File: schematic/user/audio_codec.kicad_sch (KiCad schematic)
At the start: 27 parts, among them U4 TLV320AIC3254IRHBR

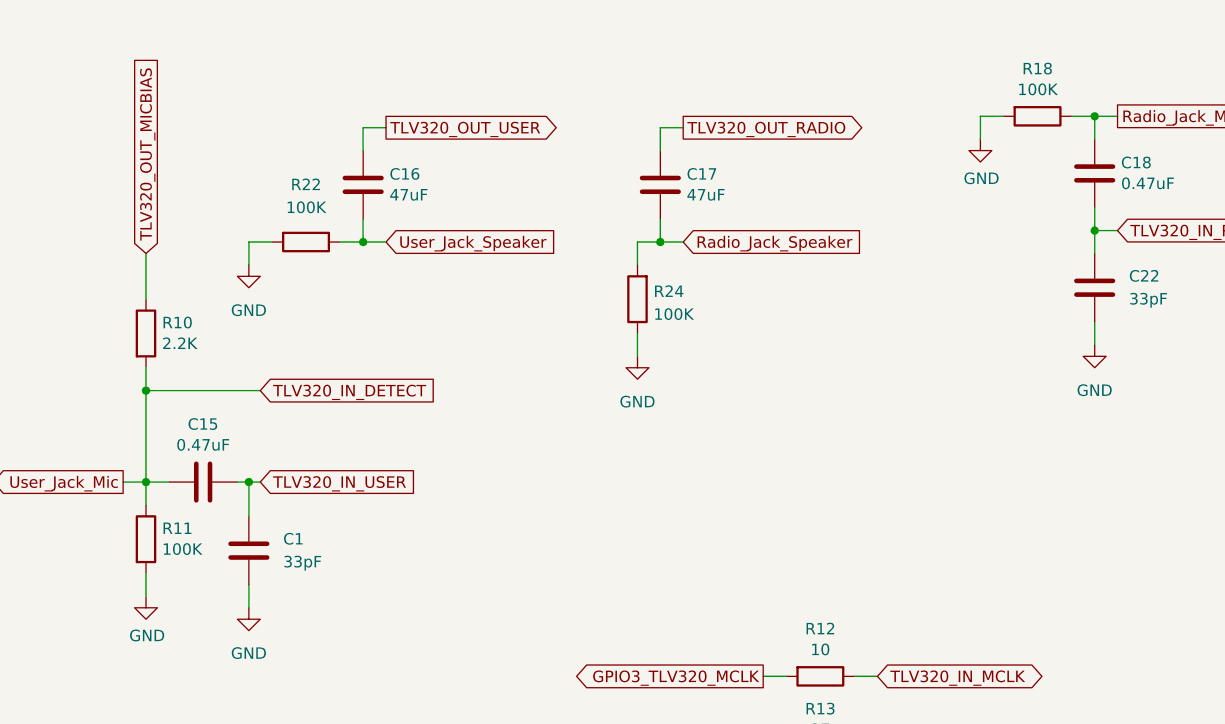
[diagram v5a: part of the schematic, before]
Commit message: v0.6 board: use 10K for audio pulldown resistors.
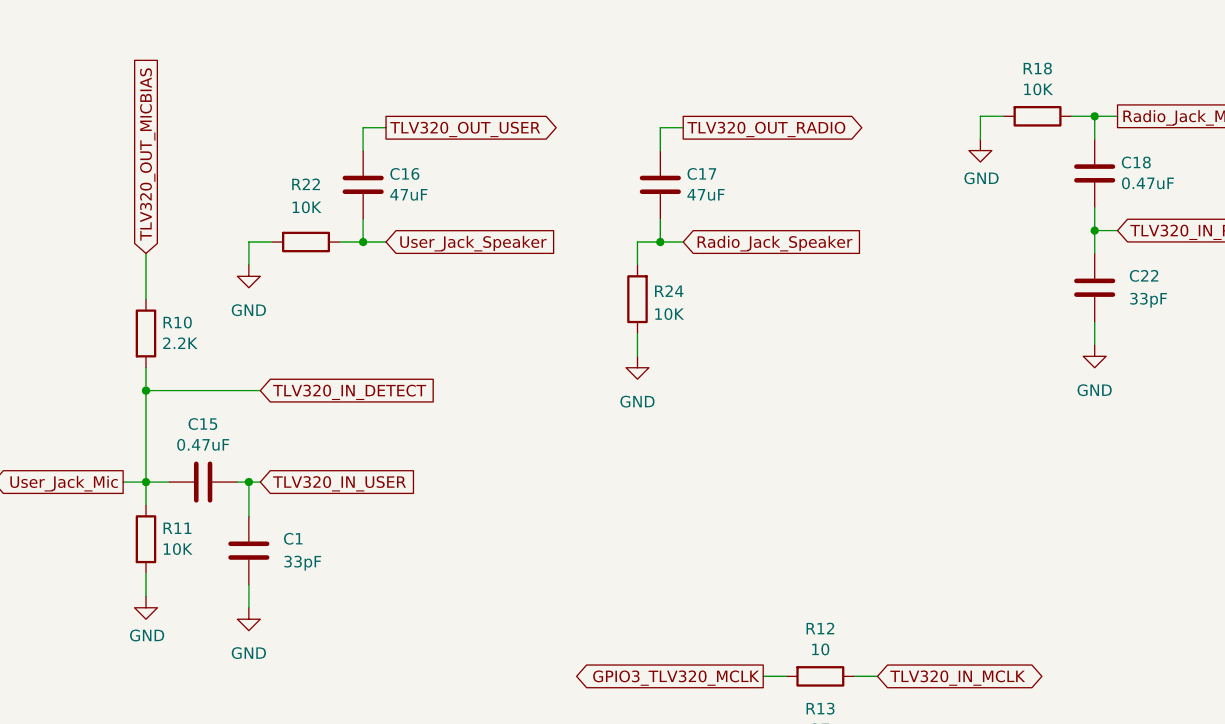
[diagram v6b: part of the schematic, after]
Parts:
- R11, R18, R22, R24: value 100K -> 10K; LCSC C25741 -> C25744
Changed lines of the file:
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@@
     (in_bom yes) (on_board yes) (fields_autoplaced)
     (property "Reference" "R22" (id 0) (at 167.64 35.56 90))
-    (property "Value" "100K" (id 1) (at 167.64 38.1 90))
+    (property "Value" "10K" (id 1) (at 167.64 38.1 90))
     (property "Footprint" "Resistor_SMD:R_0402_1005Metric" (id 2) (at 167.64 40.132 90)
       (effects (font (size 1.27 1.27)) hide)
     )
-    (property "Datasheet" "https://datasheet.lcsc.com/lcsc/2206010100_UNI-ROYAL-Uniroyal-Elec-0402WGF1003TCE_C25741.pdf" (id 3) (at 167.64 41.91 0)
-      (effects (font (size 1.27 1.27)) hide)
-    )
-    (property "LCSC" "C25741" (id 4) (at 167.64 41.91 0)
+    (property "Datasheet" "https://datasheet.lcsc.com/lcsc/2206010100_UNI-ROYAL-Uniroyal-Elec-0402WGF1002TCE_C25744.pdf" (id 3) (at 167.64 41.91 0)
+      (effects (font (size 1.27 1.27)) hide)
+    )
+    (property "LCSC" "C25744" (id 4) (at 167.64 41.91 0)
       (effects (font (size 1.27 1.27)) hide)
     )
@@
       (effects (font (size 1.27 1.27)) (justify right))
     )
-    (property "Value" "100K" (id 1) (at 206.248 49.9622 0)
+    (property "Value" "10K" (id 1) (at 206.248 49.9622 0)
       (effects (font (size 1.27 1.27)) (justify right))
     )
@@
       (effects (font (size 1.27 1.27)) hide)
     )
-    (property "Datasheet" "https://datasheet.lcsc.com/lcsc/2206010100_UNI-ROYAL-Uniroyal-Elec-0402WGF1003TCE_C25741.pdf" (id 3) (at 204.47 48.26 0)
-      (effects (font (size 1.27 1.27)) hide)
-    )
-    (property "LCSC" "C25741" (id 4) (at 204.47 48.26 0)
+    (property "Datasheet" "https://datasheet.lcsc.com/lcsc/2206010100_UNI-ROYAL-Uniroyal-Elec-0402WGF1002TCE_C25744.pdf" (id 3) (at 204.47 48.26 0)
+      (effects (font (size 1.27 1.27)) hide)
+    )
+    (property "LCSC" "C25744" (id 4) (at 204.47 48.26 0)
       (effects (font (size 1.27 1.27)) hide)
     )
@@
     (in_bom yes) (on_board yes)
     (property "Reference" "R18" (id 0) (at 248.92 22.6822 90))
-    (property "Value" "100K" (id 1) (at 248.92 24.9936 90))
+    (property "Value" "10K" (id 1) (at 248.92 24.9936 90))
     (property "Footprint" "Resistor_SMD:R_0402_1005Metric" (id 2) (at 248.92 26.162 90)
       (effects (font (size 1.27 1.27)) hide)
     )
-    (property "Datasheet" "https://datasheet.lcsc.com/lcsc/2206010100_UNI-ROYAL-Uniroyal-Elec-0402WGF1003TCE_C25741.pdf" (id 3) (at 248.92 27.94 0)
-      (effects (font (size 1.27 1.27)) hide)
-    )
-    (property "LCSC" "C25741" (id 4) (at 248.92 27.94 0)
+    (property "Datasheet" "https://datasheet.lcsc.com/lcsc/2206010100_UNI-ROYAL-Uniroyal-Elec-0402WGF1002TCE_C25744.pdf" (id 3) (at 248.92 27.94 0)
+      (effects (font (size 1.27 1.27)) hide)
+    )
+    (property "LCSC" "C25744" (id 4) (at 248.92 27.94 0)
       (effects (font (size 1.27 1.27)) hide)
     )
@@
       (effects (font (size 1.27 1.27)) (justify left))
     )
-    (property "Value" "100K" (id 1) (at 151.638 76.073 0)
+    (property "Value" "10K" (id 1) (at 151.638 76.073 0)
       (effects (font (size 1.27 1.27)) (justify left))
     )
@@
       (effects (font (size 1.27 1.27)) hide)
     )
-    (property "Datasheet" "https://datasheet.lcsc.com/lcsc/2206010100_UNI-ROYAL-Uniroyal-Elec-0402WGF1003TCE_C25741.pdf" (id 3) (at 149.86 74.93 0)
-      (effects (font (size 1.27 1.27)) hide)
-    )
-    (property "LCSC" "C25741" (id 4) (at 149.86 74.93 0)
-      (effects (font (size 1.27 1.27)) hide)
-    )
+    (property "Datasheet" "https://datasheet.lcsc.com/lcsc/2206010100_UNI-ROYAL-Uniroyal-Elec-0402WGF1002TCE_C25744.pdf" (id 3) (at 149.86 74.93 0)
+      (effects (font (size 1.27 1.27)) hide)
+    )
+    (property "LCSC" "C25744" (id 4) (at 149.86 74.93 0)
+      (effects (font (size 1.27 1.27)) hide)
+    )

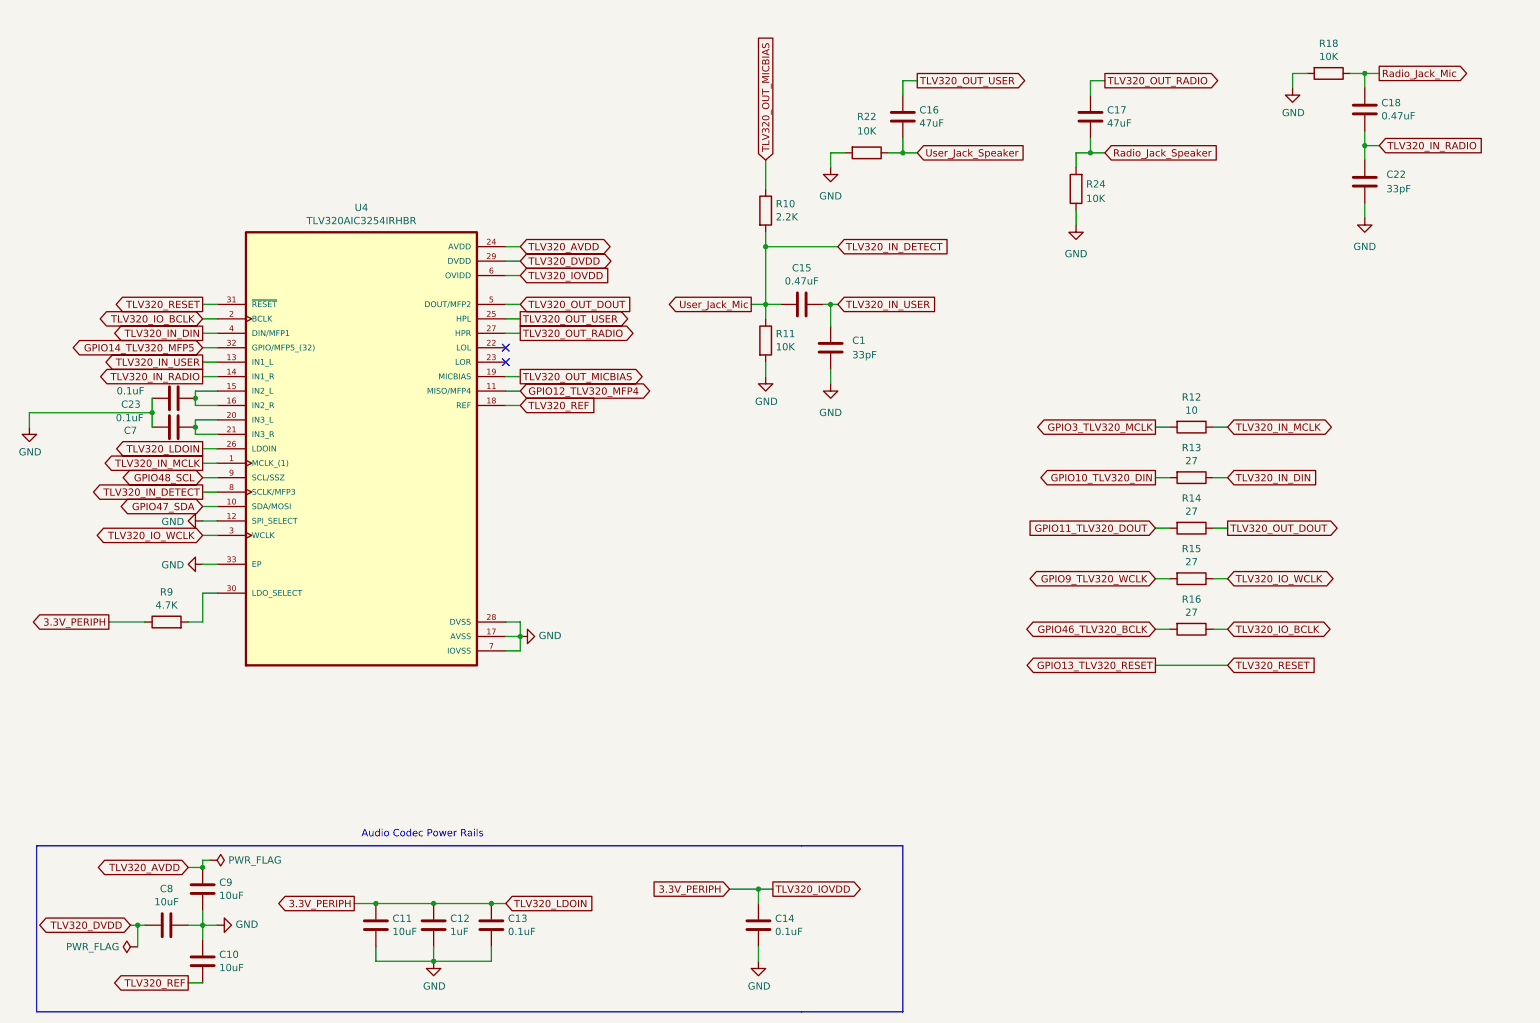
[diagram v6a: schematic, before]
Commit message: v0.7 board: add LPF on DAC outputs to avoid aliasing noise.
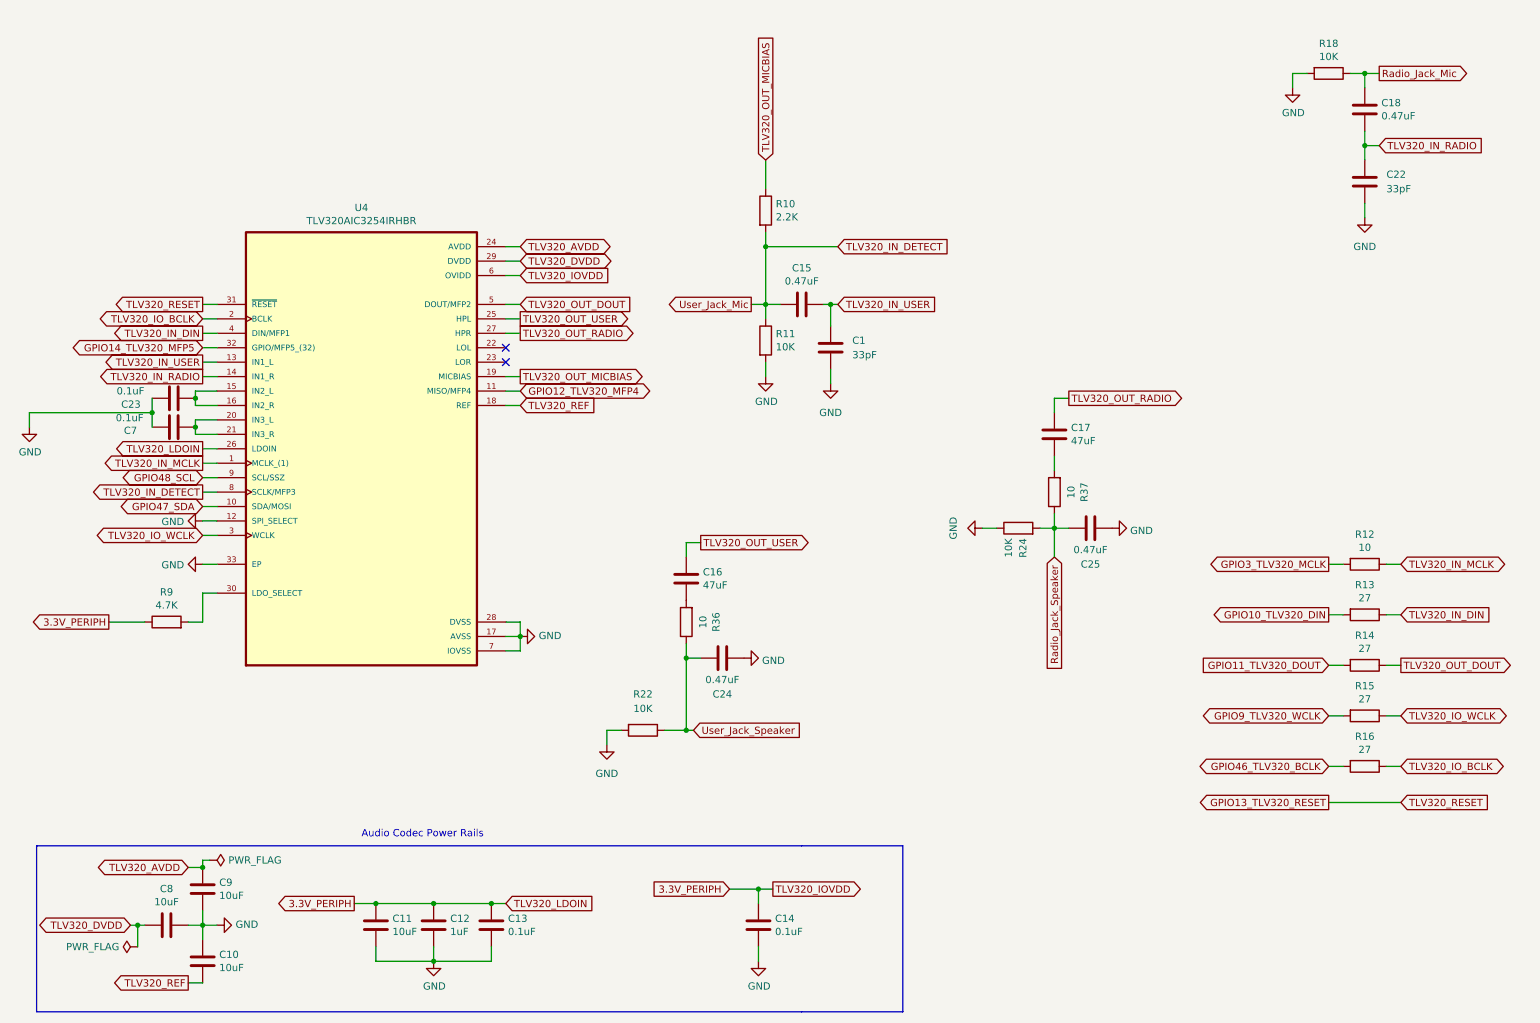
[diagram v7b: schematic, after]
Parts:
- added C24, C25: 0.47uF, Capacitor_SMD:C_0402_1005Metric, symbol Device:C
- added R36, R37: 10, Resistor_SMD:R_0402_1005Metric, symbol Device:R
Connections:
- net GND: now also C24.1, C25.1
- net Radio_Jack_Speaker: now also C25.2, R37.1; no longer C17.2
- net User_Jack_Speaker: now also C24.2, R36.1; no longer C16.2
- new net: C17.2, R37.2
- new net: C16.2, R36.2
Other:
- moved on the sheet: C16, C17, R12, R13, R14, R15, R16, R22, R24

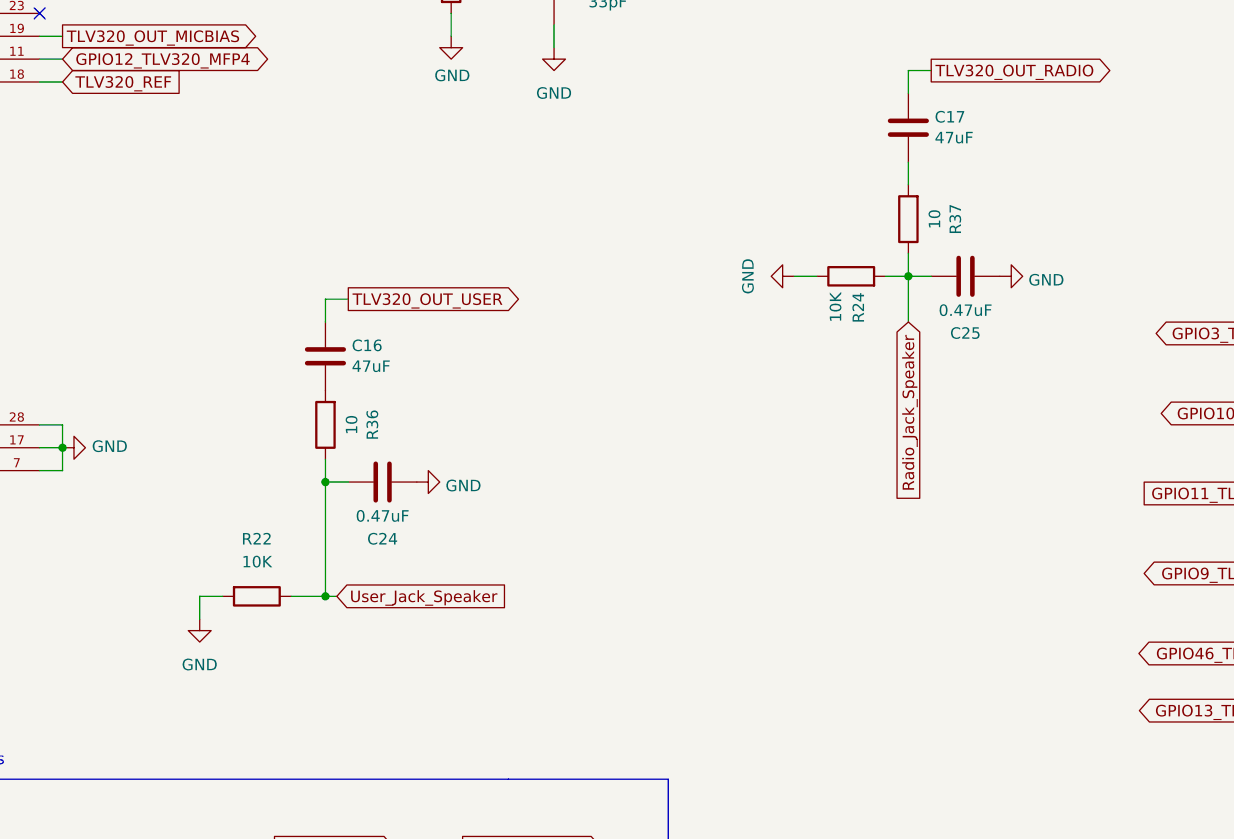
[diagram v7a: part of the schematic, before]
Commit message: v0.7 board: remove filter components as we may not actually need them.
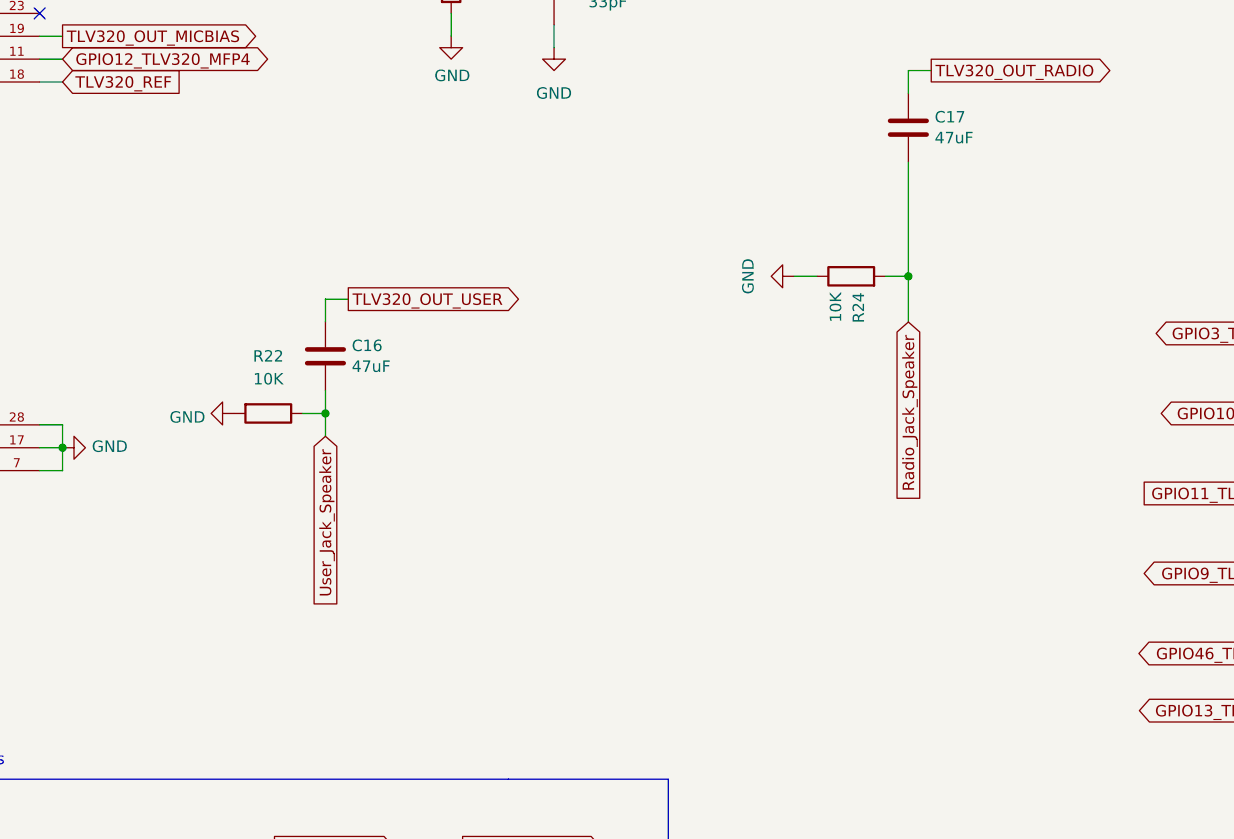
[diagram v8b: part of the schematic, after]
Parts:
- removed C24, C25: 0.47uF, Capacitor_SMD:C_0402_1005Metric, symbol Device:C
- removed R36, R37: 10, Resistor_SMD:R_0402_1005Metric, symbol Device:R
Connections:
- net Radio_Jack_Speaker: now also C17.2
- net User_Jack_Speaker: now also C16.2
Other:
- moved on the sheet: R22
